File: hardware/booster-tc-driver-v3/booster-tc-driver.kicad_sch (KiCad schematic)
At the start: 99 parts, among them IC1 CAT4109V-GT2, IC2 LDL1117S50R, J1 62201021121, J2 EHT-105-01-S-D, J3 22-23-2021, J4 3-647166-2, J5 3-647166-2, J6 3-647166-2, J7 3-647166-2, J8 3-647166-2, Q1 T2N7002AK, Q2 BUK9M5R2-30EX, SW1 SW_SPDT, U1 IF-D95T << must be T, U2 IF-E96E, U3 IF-D95T << must be T, U4 CSTNE8M00G550000R0, U5 STM32G474CBTx, U6 MCP9700Ax-ETT, U7 AP1501A-12K5G-13, U8 LT1963AxST-3.3

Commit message: v3
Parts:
- removed C23: .1uf, Capacitor_SMD:C_0603_1608Metric_Pad1.08x0.95mm_HandSolder, symbol Device:C
- removed D16: 1N5819HW-7-F, digikey-footprints:SOD-123, symbol dk_Diodes-Rectifiers-Single:1N5819HW-7-F
- removed J8: 3-647166-2, Library:36471662, symbol New_Library:3-647166-2
- added C13: .1uf, Capacitor_SMD:C_0603_1608Metric_Pad1.08x0.95mm_HandSolder, symbol Device:C
- added J11: 3-647166-5, Library:36471665, symbol New_Library:3-647166-5
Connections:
- net +24V: now also J11.3, J11.4
- net GND: now also C13.1
- net VREF: now also C13.2
- net at Q2.5 (D): now also J11.1, J11.2
- new net FAN_PWM: J11.5

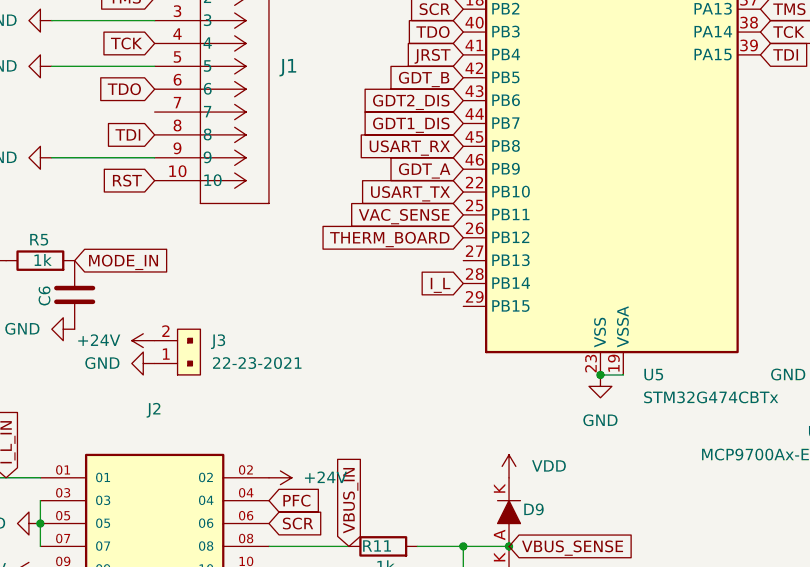
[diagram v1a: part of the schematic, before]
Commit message: v3 front silkscreen
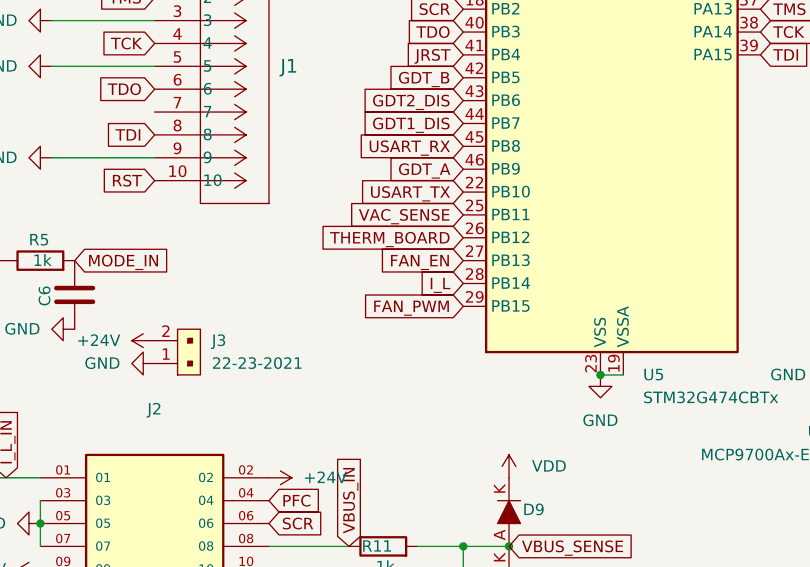
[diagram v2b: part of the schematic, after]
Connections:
- net FAN_EN: now also U5.27 (PB13)
- net FAN_PWM: now also U5.29 (PB15)
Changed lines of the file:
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@@
+		)
+	)
+	(global_label "FAN_PWM"
+		(shape input)
+		(at 83.82 133.35 180)
+		(fields_autoplaced yes)
+		(effects
+			(font
+				(size 1.27 1.27)
+			)
+			(justify right)
+		)
+		(property "Intersheetrefs" "${INTERSHEET_REFS}"
+			(at 72.1867 133.35 0)
+			(effects
+				(font
+					(size 1.27 1.27)
+				)
+				(justify right)
+				(hide yes)
+			)
 		)
 	)
@@
 				(hide yes)
 			)
+		)
+	)
+	(global_label "FAN_EN"
+		(shape input)
+		(at 83.82 128.27 180)
+		(fields_autoplaced yes)
+		(effects
+			(font
+				(size 1.27 1.27)
+			)
+			(justify right)
+		)
+		(property "Intersheetrefs" "${INTERSHEET_REFS}"
+			(at 73.88 128.27 0)
+			(effects
+				(font
+					(size 1.27 1.27)
+				)
+				(justify right)
+				(hide yes)
+			)

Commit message: pfc v3
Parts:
- added R23: 1k, Resistor_SMD:R_0603_1608Metric_Pad0.98x0.95mm_HandSolder, symbol Device:R
- added R30: 100R, Resistor_SMD:R_0603_1608Metric_Pad0.98x0.95mm_HandSolder, symbol Device:R
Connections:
- net PFC: now also R23.2; no longer J2.04
- net SCR: now also R30.2; no longer J2.06
- new net: J2.06, R30.1
- new net: J2.04, R23.1
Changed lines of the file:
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@@
 	)
 	(junction
+		(at 62.23 160.02)
+		(diameter 0)
+		(color 0 0 0 0)
+	)
+	(junction
 		(at 36.83 53.34)
 		(diameter 0)
@@
 	(wire
 		(pts
+			(xy 71.12 157.48) (xy 72.39 157.48)
+		)
+		(stroke
+			(width 0)
+			(type default)
+		)
+	)
+	(wire
+		(pts
 			(xy 50.8 39.37) (xy 50.8 44.45)
 		)
@@
 	(wire
 		(pts
+			(xy 71.12 154.94) (xy 72.39 154.94)
+		)
+		(stroke
+			(width 0)
+			(type default)
+		)
+	)
+	(wire
+		(pts
 			(xy 99.06 140.97) (xy 101.6 140.97)
 		)
@@
 	(wire
 		(pts
+			(xy 62.23 157.48) (xy 63.5 157.48)
+		)
+		(stroke
+			(width 0)
+			(type default)
+		)
+	)
+	(wire
+		(pts
 			(xy 142.24 83.82) (xy 147.32 83.82)
 		)
@@
 	(wire
 		(pts
+			(xy 62.23 160.02) (xy 62.23 161.29)
+		)
+		(stroke
+			(width 0)
+			(type default)
+		)
+	)
+	(wire
+		(pts
 			(xy 39.37 181.61) (xy 46.99 181.61)
 		)
@@
 	(wire
 		(pts
+			(xy 62.23 154.94) (xy 63.5 154.94)
+		)
+		(stroke
+			(width 0)
+			(type default)
+		)
+	)
+	(wire
+		(pts
 			(xy 45.72 194.31) (xy 45.72 185.42)
 		)
@@
 		)
 	)
+	(global_label "PFC"
+		(shape input)
+		(at 72.39 154.94 0)
+		(fields_autoplaced yes)
+		(effects
+			(font
+				(size 1.27 1.27)
+			)
+			(justify left)
+		)
+		(property "Intersheetrefs" "${INTERSHEET_REFS}"
+			(at 79.0038 154.94 0)
+			(effects
+				(font
+					(size 1.27 1.27)
+				)
+				(justify left)
+				(hide yes)
+			)
+		)
+	)
 	(global_label "USART_TX"
 		(shape input)
@@
 		)
 	)
-	(global_label "VBUS_IN"
+	(global_label "SCR"
 		(shape input)
-		(at 71.12 160.02 90)
+		(at 72.39 157.48 0)
 		(fields_autoplaced yes)
 		(effects
@@
 		)
 		(property "Intersheetrefs" "${INTERSHEET_REFS}"
-			(at 71.12 149.2333 90)
+			(at 79.1247 157.48 0)
 			(effects
 				(font
@@
 		)
 	)
-	(global_label "SCR"
-		(shape input)
-		(at 62.23 157.48 0)
-		(fields_autoplaced yes)
-		(effects
-			(font
-				(size 1.27 1.27)
-			)
-			(justify left)
-		)
-		(property "Intersheetrefs" "${INTERSHEET_REFS}"
-			(at 68.9647 157.48 0)
-			(effects
-				(font
-					(size 1.27 1.27)
-				)
-				(justify left)
-				(hide yes)
-			)
-		)
-	)
-	(global_label "PFC"
-		(shape input)
-		(at 62.23 154.94 0)
-		(fields_autoplaced yes)
-		(effects
-			(font
-				(size 1.27 1.27)
-			)
-			(justify left)
-		)
-		(property "Intersheetrefs" "${INTERSHEET_REFS}"
-			(at 68.8438 154.94 0)
-			(effects
-				(font
-					(size 1.27 1.27)
-				)
-				(justify left)
-				(hide yes)
-			)
-		)
-	)
 	(global_label "VBUS_SENSE"
 		(shape input)
@@
 		)
 	)
+	(global_label "VBUS_IN"
+		(shape input)
+		(at 62.23 161.29 0)
+		(fields_autoplaced yes)
+		(effects
+			(font
+				(size 1.27 1.27)
+			)
+			(justify left)
+		)
+		(property "Intersheetrefs" "${INTERSHEET_REFS}"
+			(at 73.0167 161.29 0)
+			(effects
+				(font
+					(size 1.27 1.27)
+				)
+				(justify left)
+				(hide yes)
+			)
+		)
+	)
 	(symbol
 		(lib_id "Device:C")
@@
 	)
 	(symbol
+		(lib_id "Device:R")
+		(at 67.31 157.48 90)
+		(unit 1)
+		(exclude_from_sim no)
+		(in_bom yes)
+		(on_board yes)
+		(dnp no)
+		(property "Reference" "R30"
+			(at 68.326 157.48 90)
+			(effects
+				(font
+					(size 1.27 1.27)
+				)
+				(justify left)
+			)
+		)
+		(property "Value" "100R"
+			(at 68.58 159.766 90)
+			(effects
+				(font
+					(size 1.27 1.27)
+				)
+				(justify left)
+			)
+		)
+		(property "Footprint" "Resistor_SMD:R_0603_1608Metric_Pad0.98x0.95mm_HandSolder"
+			(at 67.31 159.258 90)
+			(effects
+				(font
+					(size 1.27 1.27)
+				)
+				(hide yes)
+			)
+		)
+		(property "Datasheet" "~"
+			(at 67.31 157.48 0)
+			(effects
+				(font
+					(size 1.27 1.27)
+				)
+				(hide yes)
+			)
+		)
+		(property "Description" "Resistor"
+			(at 67.31 157.48 0)
+			(effects
+				(font
+					(size 1.27 1.27)
+				)
+				(hide yes)
+			)
+		)
+		(pin "1"
+		)
+		(pin "2"
+		)
+		(instances
+			(project "booster-tc-driver"
+				(path "/3c175d5e-f31a-4933-a865-8318878a5034"
+					(reference "R30")
+					(unit 1)
+				)
+			)
+		)
+	)
+	(symbol
 		(lib_id "Device:C")
 		(at 46.99 177.8 0)
@@
 					(unit 1)
 				)
+			)
+		)
+	)
+	(symbol
+		(lib_id "Device:R")
+		(at 67.31 154.94 90)
+		(unit 1)
+		(exclude_from_sim no)
+		(in_bom yes)
+		(on_board yes)
+		(dnp no)
+		(property "Reference" "R23"
+			(at 68.326 154.94 90)
+			(effects
+				(font
+					(size 1.27 1.27)
+				)
+				(justify left)
+			)
+		)
+		(property "Value" "1k"
+			(at 68.58 157.226 90)
+			(effects
+				(font
+					(size 1.27 1.27)
+				)
+				(justify left)
+			)
+		)
+		(property "Footprint" "Resistor_SMD:R_0603_1608Metric_Pad0.98x0.95mm_HandSolder"
+			(at 67.31 156.718 90)
+			(effects
+				(font
+					(size 1.27 1.27)
+				)
+				(hide yes)
+			)
+		)
+		(property "Datasheet" "~"
+			(at 67.31 154.94 0)
+			(effects
+				(font
+					(size 1.27 1.27)
+				)
+				(hide yes)
+			)
+		)
+		(property "Description" "Resistor"
+			(at 67.31 154.94 0)
+			(effects
+				(font
+					(size 1.27 1.27)
+				)
+				(hide yes)
+			)
+		)
+		(pin "1"
+		)
+		(pin "2"
+		)
+		(instances
+			(project "booster-tc-driver"
+				(path "/3c175d5e-f31a-4933-a865-8318878a5034"
+					(reference "R23")
+					(unit 1)
+				)

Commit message: pfc v3 finalized
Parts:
- removed C13: .1uf, Capacitor_SMD:C_0603_1608Metric_Pad1.08x0.95mm_HandSolder, symbol Device:C
- removed D10, D7: 1N5819HW-7-F, digikey-footprints:SOD-123, symbol dk_Diodes-Rectifiers-Single:1N5819HW-7-F
- removed J2: EHT-105-01-S-D, Library:SAMTEC_EHT-105-01-S-D, symbol EHT-105-01-S-D:EHT-105-01-S-D
- removed R10: 1k, Resistor_SMD:R_0603_1608Metric_Pad0.98x0.95mm_HandSolder, symbol Device:R
- added J2: 61201021621, Connector_IDC:IDC-Header_2x05_P2.54mm_Vertical, symbol Connector_Generic:Conn_02x05_Odd_Even
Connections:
- net +24V: now also J2.1 (Pin_1)
- net +5V: now also J2.9 (Pin_9)
- net GND: now also J2.3 (Pin_3), J2.5 (Pin_5), J2.7 (Pin_7)
- net I_L_IN: now also J2.2 (Pin_2)
- net VAC_IN: now also J2.10 (Pin_10)
- net VBUS_IN: now also J2.8 (Pin_8)
- net at R30.1: now also J2.6 (Pin_6)
- net at R23.1: now also J2.4 (Pin_4)
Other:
- moved on the sheet: C11, C3, D1, R1

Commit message: idk
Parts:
- C6, C9: value 1u -> 2u2
